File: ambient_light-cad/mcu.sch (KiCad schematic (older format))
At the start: 26 parts

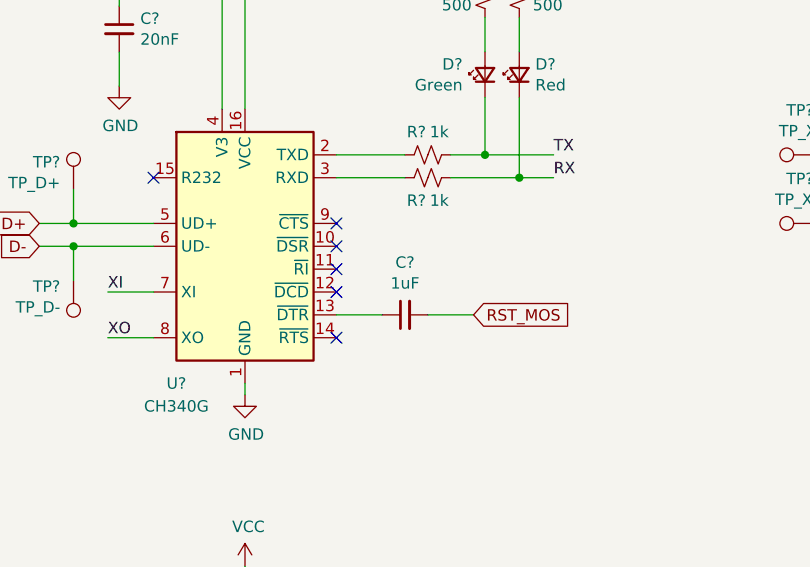
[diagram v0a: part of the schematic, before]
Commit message: [Updated] Symbol field for PCB layout
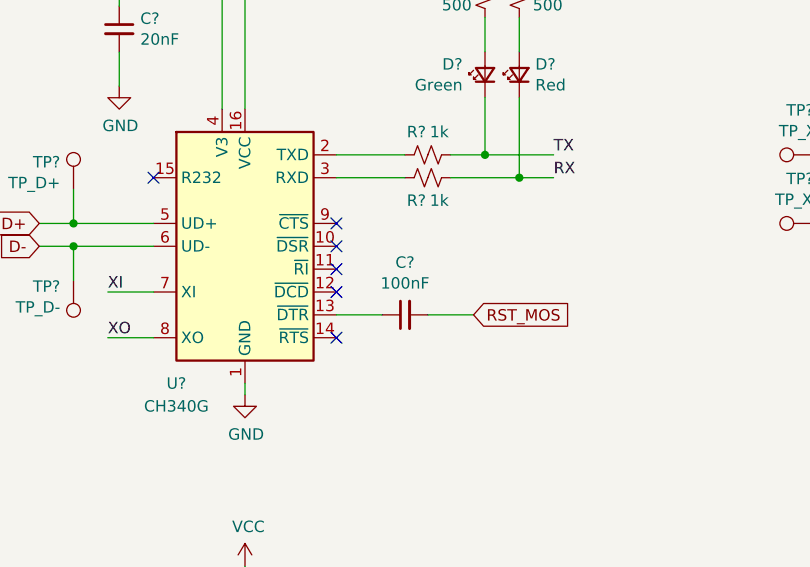
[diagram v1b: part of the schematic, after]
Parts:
- C? (x6): footprint (none) -> Capacitor_SMD:C_0603_1608Metric_Pad1.08x0.95mm_HandSolder
- C?: value 1uF -> 100nF; footprint (none) -> Capacitor_SMD:C_0603_1608Metric_Pad1.08x0.95mm_HandSolder
- D? (x3): footprint (none) -> LED_SMD:LED_0603_1608Metric_Pad1.05x0.95mm_HandSolder
- R? (x5): footprint (none) -> Resistor_SMD:R_0603_1608Metric_Pad0.98x0.95mm_HandSolder
- TP? (x7): footprint (none) -> TestPoint:TestPoint_Pad_D2.0mm
- Y? (x2): footprint (none) -> Crystal:Crystal_SMD_0603-4Pin_6.0x3.5mm_HandSoldering
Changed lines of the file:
@@
 F 0 "C?" H 1342 4846 50  0000 L CNN
 F 1 "100nF" H 1342 4755 50  0000 L CNN
-F 2 "" H 1250 4800 50  0001 C CNN
+F 2 "Capacitor_SMD:C_0603_1608Metric_Pad1.08x0.95mm_HandSolder" H 1250 4800 50  0001 C CNN
 F 3 "~" H 1250 4800 50  0001 C CNN
 	1    1250 4800
@@
 F 0 "R?" V 3250 1900 50  0000 C CNN
 F 1 "1k" V 3250 2000 50  0000 C CNN
-F 2 "" H 3350 1950 50  0001 C CNN
+F 2 "Resistor_SMD:R_0603_1608Metric_Pad0.98x0.95mm_HandSolder" H 3350 1950 50  0001 C CNN
 F 3 "~" H 3350 1950 50  0001 C CNN
 	1    3350 1950
@@
 F 0 "Y?" V 5700 3900 50  0000 L CNN
 F 1 "14.4756MHz" V 5800 3900 50  0000 L CNN
-F 2 "" H 5900 4400 50  0001 C CNN
+F 2 "Crystal:Crystal_SMD_0603-4Pin_6.0x3.5mm_HandSoldering" H 5900 4400 50  0001 C CNN
 F 3 "~" H 5900 4400 50  0001 C CNN
 	1    5900 4400
@@
 F 0 "D?" V 3646 1698 50  0000 L CNN
 F 1 "Green" V 3555 1698 50  0000 L CNN
-F 2 "" V 3600 1600 50  0001 C CNN
+F 2 "LED_SMD:LED_0603_1608Metric_Pad1.05x0.95mm_HandSolder" V 3600 1600 50  0001 C CNN
 F 3 "~" V 3600 1600 50  0001 C CNN
 	1    3600 1600
@@
 F 0 "R?" H 3809 1296 50  0000 L CNN
 F 1 "500" H 3809 1205 50  0000 L CNN
-F 2 "" H 3750 1250 50  0001 C CNN
+F 2 "Resistor_SMD:R_0603_1608Metric_Pad0.98x0.95mm_HandSolder" H 3750 1250 50  0001 C CNN
 F 3 "~" H 3750 1250 50  0001 C CNN
 	1    3750 1250
@@
 F 0 "R?" H 3542 1296 50  0000 R CNN
 F 1 "500" H 3542 1205 50  0000 R CNN
-F 2 "" H 3600 1250 50  0001 C CNN
+F 2 "Resistor_SMD:R_0603_1608Metric_Pad0.98x0.95mm_HandSolder" H 3600 1250 50  0001 C CNN
 F 3 "~" H 3600 1250 50  0001 C CNN
 	1    3600 1250
@@
 F 0 "R?" H 4009 5196 50  0000 L CNN
 F 1 "1k" H 4009 5105 50  0000 L CNN
-F 2 "" H 3950 5150 50  0001 C CNN
+F 2 "Resistor_SMD:R_0603_1608Metric_Pad0.98x0.95mm_HandSolder" H 3950 5150 50  0001 C CNN
 F 3 "~" H 3950 5150 50  0001 C CNN
 	1    3950 5150
@@
 F 0 "D?" V 3996 5480 50  0000 R CNN
 F 1 "Yellow" V 3905 5480 50  0000 R CNN
-F 2 "" V 3950 5550 50  0001 C CNN
+F 2 "LED_SMD:LED_0603_1608Metric_Pad1.05x0.95mm_HandSolder" V 3950 5550 50  0001 C CNN
 F 3 "~" V 3950 5550 50  0001 C CNN
 	1    3950 5550
@@
 F 0 "D?" V 3796 1530 50  0000 R CNN
 F 1 "Red" V 3705 1530 50  0000 R CNN
-F 2 "" V 3750 1600 50  0001 C CNN
+F 2 "LED_SMD:LED_0603_1608Metric_Pad1.05x0.95mm_HandSolder" V 3750 1600 50  0001 C CNN
 F 3 "~" V 3750 1600 50  0001 C CNN
 	1    3750 1600
@@
 F 0 "C?" H 5950 2450 50  0000 L CNN
 F 1 "18pF" H 5850 2350 50  0000 L CNN
-F 2 "" H 5850 2450 50  0001 C CNN
+F 2 "Capacitor_SMD:C_0603_1608Metric_Pad1.08x0.95mm_HandSolder" H 5850 2450 50  0001 C CNN
 F 3 "~" H 5850 2450 50  0001 C CNN
 	1    5850 2450
@@
 F 0 "C?" H 6350 2450 50  0000 L CNN
 F 1 "18pF" H 6250 2350 50  0000 L CNN
-F 2 "" H 6250 2450 50  0001 C CNN
+F 2 "Capacitor_SMD:C_0603_1608Metric_Pad1.08x0.95mm_HandSolder" H 6250 2450 50  0001 C CNN
 F 3 "~" H 6250 2450 50  0001 C CNN
 	1    6250 2450
@@
 F 0 "C?" H 2092 1446 50  0000 L CNN
 F 1 "20nF" H 2092 1355 50  0000 L CNN
-F 2 "" H 2000 1400 50  0001 C CNN
+F 2 "Capacitor_SMD:C_0603_1608Metric_Pad1.08x0.95mm_HandSolder" H 2000 1400 50  0001 C CNN
 F 3 "~" H 2000 1400 50  0001 C CNN
 	1    2000 1400
@@
 AR Path="/5FD145BE/5FD4C0CA" Ref="C?"  Part="1"
 F 0 "C?" V 3479 2650 50  0000 C CNN
-F 1 "1uF" V 3388 2650 50  0000 C CNN
-F 2 "" H 3250 2650 50  0001 C CNN
+F 1 "100nF" V 3388 2650 50  0000 C CNN
+F 2 "Capacitor_SMD:C_0603_1608Metric_Pad1.08x0.95mm_HandSolder" H 3250 2650 50  0001 C CNN
 F 3 "~" H 3250 2650 50  0001 C CNN
 	1    3250 2650
@@
 F 0 "C?" H 6000 5000 50  0000 L CNN
 F 1 "18pF" H 5900 4900 50  0000 L CNN
-F 2 "" H 5900 5000 50  0001 C CNN
+F 2 "Capacitor_SMD:C_0603_1608Metric_Pad1.08x0.95mm_HandSolder" H 5900 5000 50  0001 C CNN
 F 3 "~" H 5900 5000 50  0001 C CNN
 	1    5900 5000
@@
 F 0 "C?" H 6400 5000 50  0000 L CNN
 F 1 "18pF" H 6300 4900 50  0000 L CNN
-F 2 "" H 6300 5000 50  0001 C CNN
+F 2 "Capacitor_SMD:C_0603_1608Metric_Pad1.08x0.95mm_HandSolder" H 6300 5000 50  0001 C CNN
 F 3 "~" H 6300 5000 50  0001 C CNN
 	1    6300 5000
@@
 F 0 "Y?" V 5650 1550 50  0000 L CNN
 F 1 "12MHz" V 5750 1550 50  0000 L CNN
-F 2 "" H 5850 1850 50  0001 C CNN
+F 2 "Crystal:Crystal_SMD_0603-4Pin_6.0x3.5mm_HandSoldering" H 5850 1850 50  0001 C CNN
 F 3 "~" H 5850 1850 50  0001 C CNN
 	1    5850 1850
@@
 F 0 "R?" V 3450 2000 50  0000 C CNN
 F 1 "1k" V 3450 2100 50  0000 C CNN
-F 2 "" H 3350 2050 50  0001 C CNN
+F 2 "Resistor_SMD:R_0603_1608Metric_Pad0.98x0.95mm_HandSolder" H 3350 2050 50  0001 C CNN
 F 3 "~" H 3350 2050 50  0001 C CNN
 	1    3350 2050
@@
 F 0 "TP?" V 4905 4572 50  0000 C CNN
 F 1 "TP_XTAL1" V 4996 4572 50  0000 C CNN
-F 2 "" H 5300 4500 50  0001 C CNN
+F 2 "TestPoint:TestPoint_Pad_D2.0mm" H 5300 4500 50  0001 C CNN
 F 3 "~" H 5300 4500 50  0001 C CNN
 	1    5100 4500
@@
 F 0 "TP?" V 4905 4872 50  0000 C CNN
 F 1 "TP_XTAL2" V 4996 4872 50  0000 C CNN
-F 2 "" H 5300 4800 50  0001 C CNN
+F 2 "TestPoint:TestPoint_Pad_D2.0mm" H 5300 4800 50  0001 C CNN
 F 3 "~" H 5300 4800 50  0001 C CNN
 	1    5100 4800
@@
 F 0 "TP?" V 4855 2022 50  0000 C CNN
 F 1 "TP_XI" V 4946 2022 50  0000 C CNN
-F 2 "" H 5250 1950 50  0001 C CNN
+F 2 "TestPoint:TestPoint_Pad_D2.0mm" H 5250 1950 50  0001 C CNN
 F 3 "~" H 5250 1950 50  0001 C CNN
 	1    5050 1950
@@
 F 0 "TP?" V 4855 2322 50  0000 C CNN
 F 1 "TP_XO" V 4946 2322 50  0000 C CNN
-F 2 "" H 5250 2250 50  0001 C CNN
+F 2 "TestPoint:TestPoint_Pad_D2.0mm" H 5250 2250 50  0001 C CNN
 F 3 "~" H 5250 2250 50  0001 C CNN
 	1    5050 2250
@@
 F 0 "TP?" H 3292 5868 50  0000 R CNN
 F 1 "TP_RST" H 3292 5777 50  0000 R CNN
-F 2 "" H 3550 5750 50  0001 C CNN
+F 2 "TestPoint:TestPoint_Pad_D2.0mm" H 3550 5750 50  0001 C CNN
 F 3 "~" H 3550 5750 50  0001 C CNN
 	1    3350 5750
@@
 F 0 "TP?" H 1858 2218 50  0000 L CNN
 F 1 "TP_D+" H 1858 2127 50  0000 L CNN
-F 2 "" H 2000 2100 50  0001 C CNN
+F 2 "TestPoint:TestPoint_Pad_D2.0mm" H 2000 2100 50  0001 C CNN
 F 3 "~" H 2000 2100 50  0001 C CNN
 	1    1800 2100
@@
 F 0 "TP?" H 1742 2526 50  0000 R CNN
 F 1 "TP_D-" H 1742 2617 50  0000 R CNN
-F 2 "" H 2000 2500 50  0001 C CNN
+F 2 "TestPoint:TestPoint_Pad_D2.0mm" H 2000 2500 50  0001 C CNN
 F 3 "~" H 2000 2500 50  0001 C CNN
 	1    1800 2500

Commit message: ICSP PinSocket to PinHeader
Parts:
- R? (x2): footprint Resistor_SMD:R_0603_1608Metric_Pad0.98x0.95mm_HandSolder -> Resistor_SMD:R_0603_1608Metric_Pad1.05x0.95mm_HandSolder
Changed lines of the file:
@@
 F 0 "R?" H 3809 1296 50  0000 L CNN
 F 1 "500" H 3809 1205 50  0000 L CNN
-F 2 "Resistor_SMD:R_0603_1608Metric_Pad0.98x0.95mm_HandSolder" H 3750 1250 50  0001 C CNN
+F 2 "Resistor_SMD:R_0603_1608Metric_Pad1.05x0.95mm_HandSolder" H 3750 1250 50  0001 C CNN
 F 3 "~" H 3750 1250 50  0001 C CNN
 	1    3750 1250
@@
 F 0 "R?" H 3542 1296 50  0000 R CNN
 F 1 "500" H 3542 1205 50  0000 R CNN
-F 2 "Resistor_SMD:R_0603_1608Metric_Pad0.98x0.95mm_HandSolder" H 3600 1250 50  0001 C CNN
+F 2 "Resistor_SMD:R_0603_1608Metric_Pad1.05x0.95mm_HandSolder" H 3600 1250 50  0001 C CNN
 F 3 "~" H 3600 1250 50  0001 C CNN
 	1    3600 1250
